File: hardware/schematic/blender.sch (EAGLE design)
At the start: 102 parts, among them IC1 MEGA32-A, IC2 AD7793, Q1 IRF540, Q10 IRF540, Q2 IRF540, Q5 BS170, Q6 BS170, Q7 BS170, Q8 BS170, Q9 BS170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

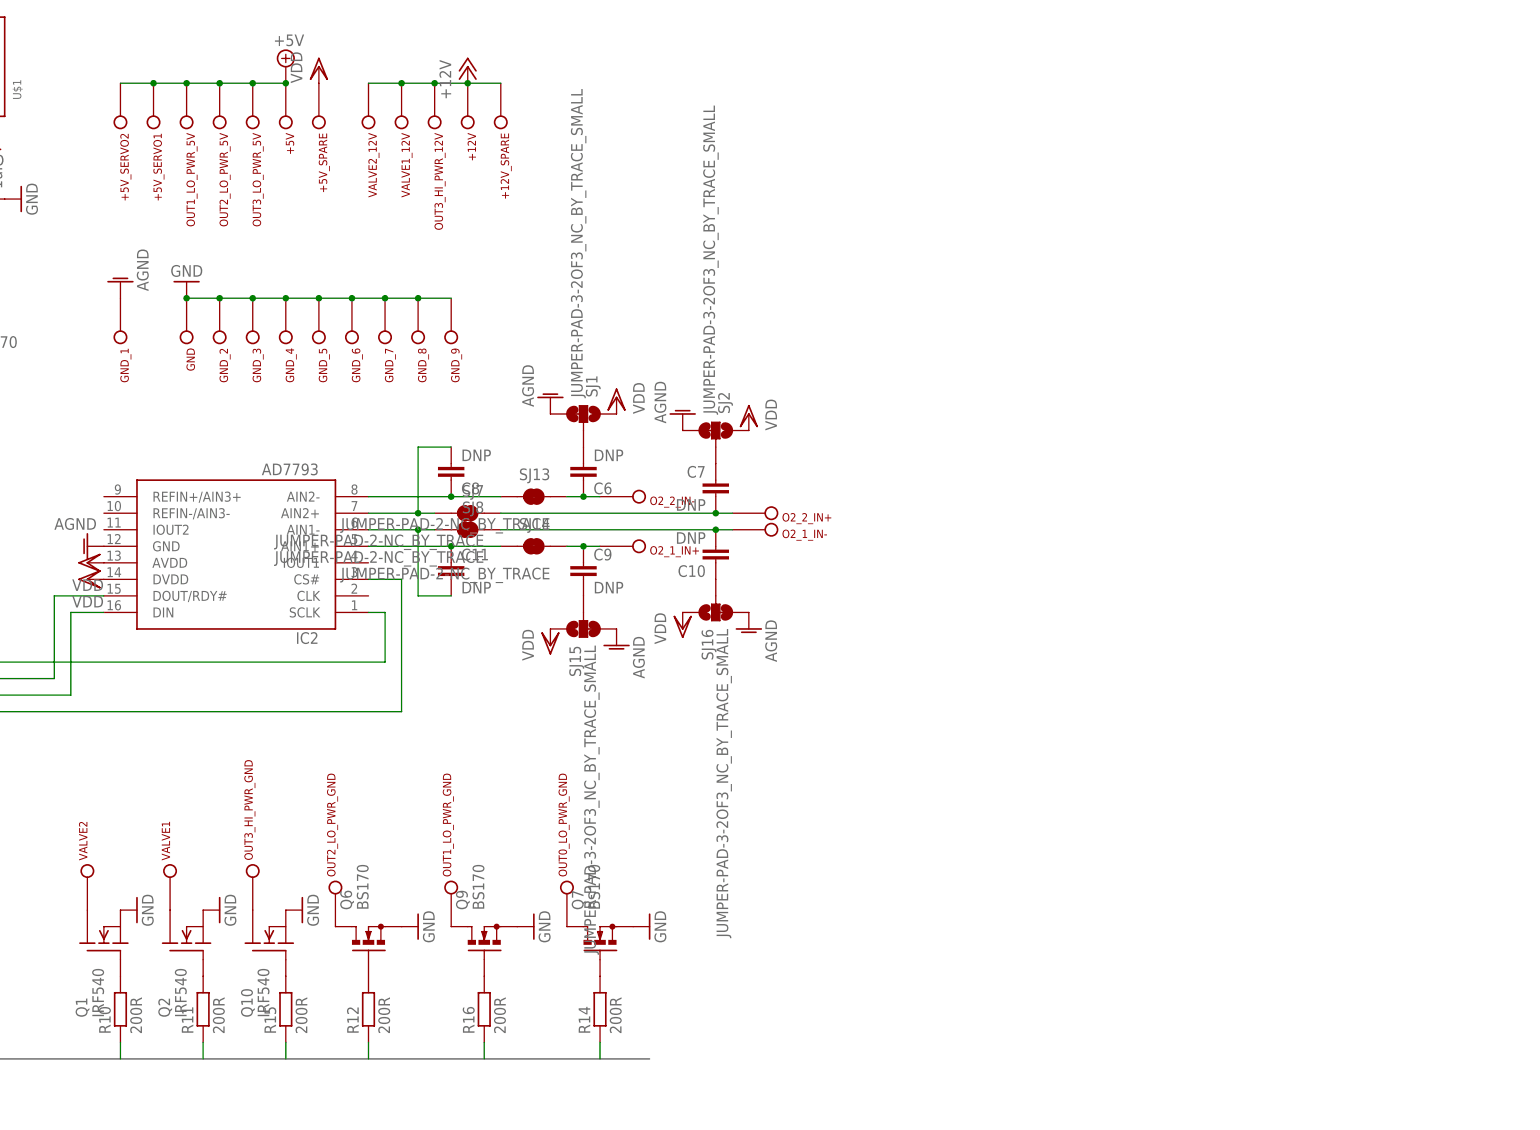
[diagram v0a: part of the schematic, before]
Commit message: some tweaks for schematic (board destroyed), added TODOs for sch (inside sch)
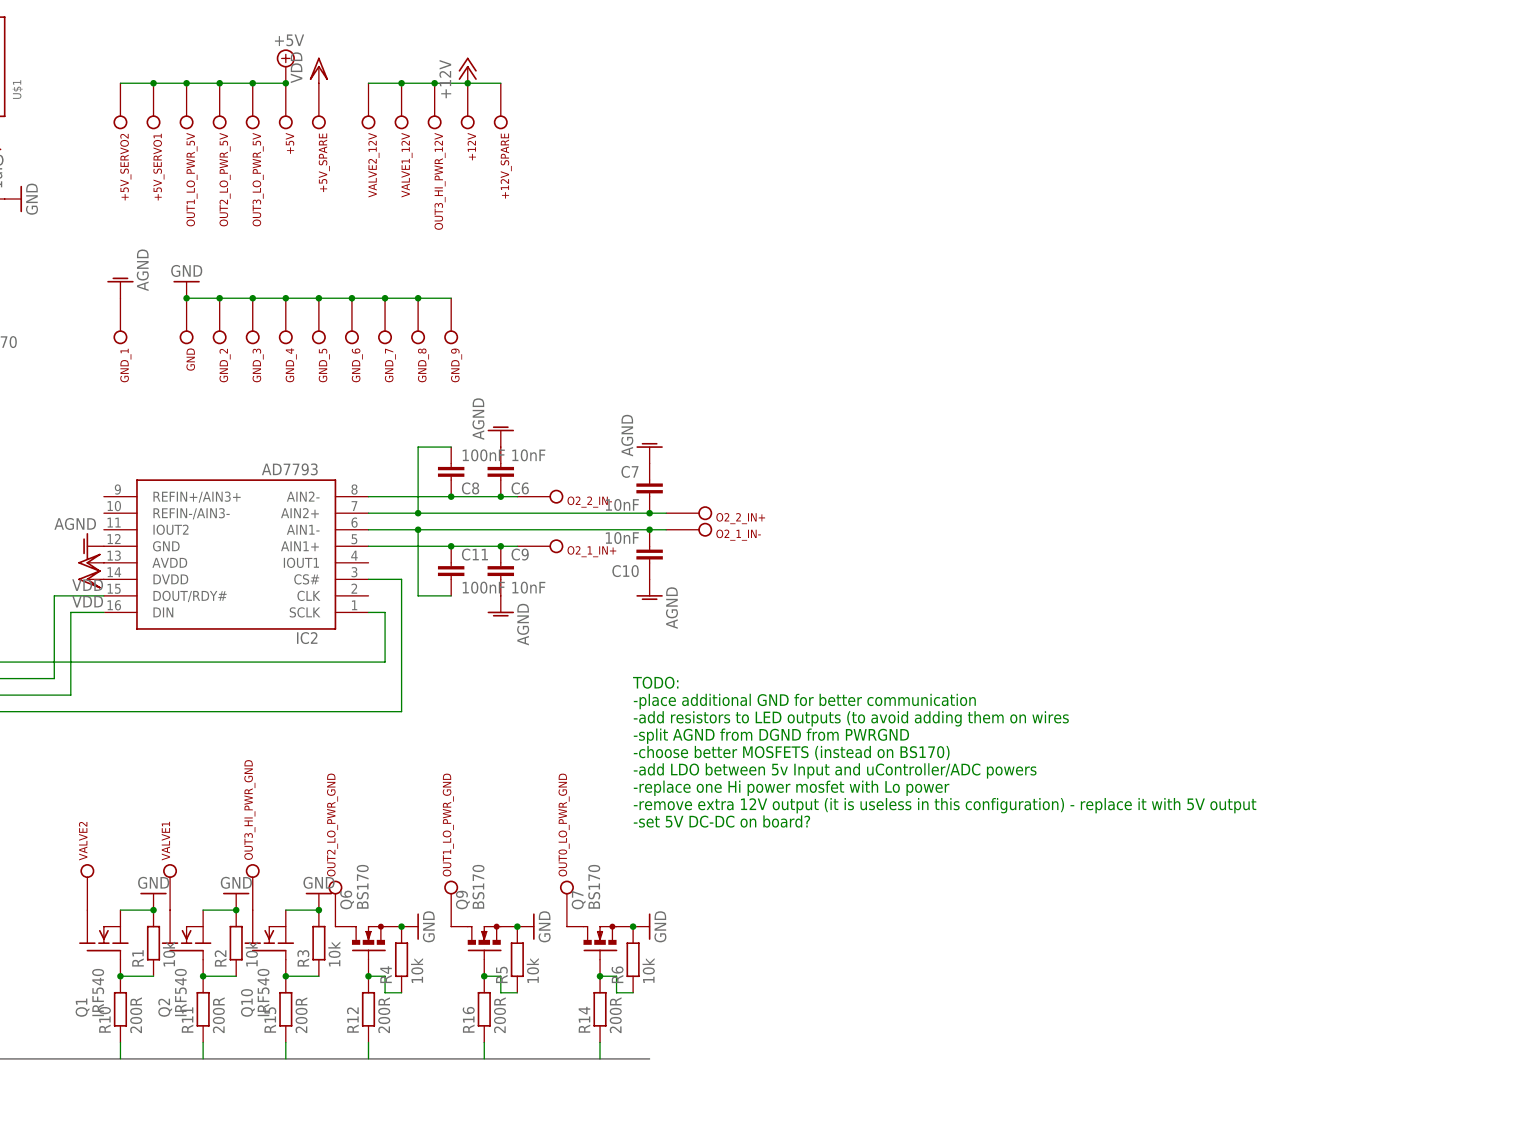
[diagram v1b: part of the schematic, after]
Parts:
- removed SJ1, SJ15, SJ16, SJ2: JUMPER-PAD-3-2OF3_NC_BY_TRACE_SMALL, SparkFun-Passives:JUMPER-PAD-3-2OF3_NC_BY_TRACE_SMALL
- removed SJ13, SJ14, SJ7, SJ8: JUMPER-PAD-2-NC_BY_TRACE, SparkFun-Passives:JUMPER-PAD-2-NC_BY_TRACE
- added R1, R2, R3, R4, R5, R6: 10k, resistor:R-EU_R0603
- C10, C6, C7, C9: value DNP -> 10nF
- C11, C8: value DNP -> 100nF
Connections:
- removed net N$1: C9.2, SJ15.2
- removed net N$2: C10.1, SJ16.2
- removed net N$3: C6.2, SJ1.2
- removed net N$56: C11.1, IC2.AIN1+, SJ14.2
- removed net N$57: C8.2, IC2.AIN2+, SJ7.2
- removed net N$58: C8.1, IC2.AIN2-, SJ13.2
- removed net N$62: C10.2, O2_1_IN-.P, SJ8.1
- removed net N$9: C7.1, SJ2.2
- net AGND: now also C10.1, C6.2, C7.1, C9.2; no longer SJ1.3, SJ15.3, SJ16.3, SJ2.3
- net GND: now also R1.2, R2.2, R3.2, R4.2, R5.2, R6.2
- net N$27: now also R1.1
- net N$28: now also R2.1
- net N$29: now also R3.1
- net N$31: now also R6.1
- net N$32: now also R4.1
- net N$33: now also R5.1
- net N$55: now also C10.2, O2_1_IN-.P; no longer SJ8.2
- net N$59: now also C8.2, IC2.AIN2+; no longer SJ7.1
- net N$60: now also C8.1, IC2.AIN2-; no longer SJ13.1
- net N$64: now also C11.1, IC2.AIN1+; no longer SJ14.1
- net VDD: no longer SJ1.1, SJ15.1, SJ16.1, SJ2.1
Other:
- note added: "TODO: -place additional GND for better communication -add resistors to LED outputs (to avoid adding them on wires -split AGND from DGND from PWRGND -choose better MOSFETS (instead on BS170) -add LDO between 5v Input and uController/ADC powers -replace one Hi power mosfet with Lo power -remove extra 12V output (it is useless in this configuration) - replace it with 5V output -set 5V DC-DC on board?"
- moved on the sheet: C10, C6, C7, C9, O2_1_IN+, O2_1_IN-, O2_2_IN+, O2_2_IN-
